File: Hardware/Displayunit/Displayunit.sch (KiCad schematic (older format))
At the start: 120 parts, among them IC1 TSC2007, IC2 MX25LM51245GXDI00, IC3 IS66WVH8M8BLL-100B1LI_0, J1 8P8C_Shielded, J2 8P8C_Shielded, J3 54104-4031, J4 Conn_ARM_JTAG_SWD_20, J5 52271-0679, J6 Conn_02x06_Odd_Even, J7 WAGO_Klemmleiste_2-pol, J8 USB_B_Micro, J9 Conn_02x05_Odd_Even, Q1 2N7002, SW1 Boot, SW2 Reset, U1 STM32L4R9ZITx, U2 USBLC6-2SC6, U3 STLD40D, U4 MAX17572, U5 MAX17572, U6 SN65HVD231, U7 AT25xxx, Y1 16 MHz, Y2 32.768

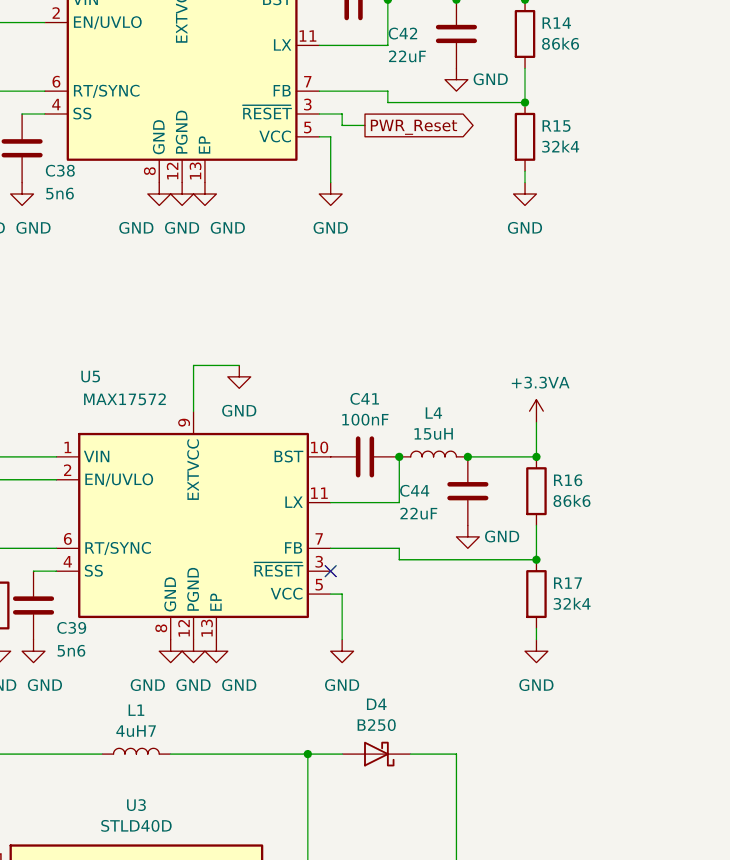
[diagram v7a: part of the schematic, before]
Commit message: Fix: behinderten Masse Bug an 3v3 Regler Mainunit und Displayboard
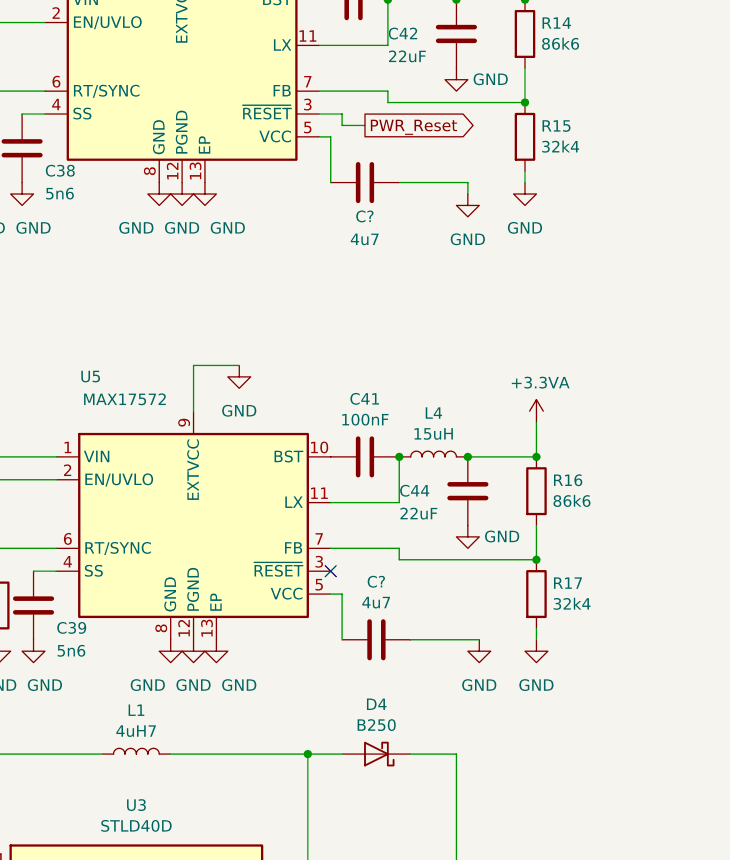
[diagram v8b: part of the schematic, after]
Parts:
- added C? (x2): 4u7, Capacitor_SMD:C_0603_1608Metric, symbol Displayunit-rescue:C-Device
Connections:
- net GND: now also C?.1, C?.1; no longer U4.5 (VCC), U5.5 (VCC)
- new net: C?.2, U4.5 (VCC)
- new net: C?.2, U5.5 (VCC)
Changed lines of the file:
@@
 EESchema Schematic File Version 4
 LIBS:Displayunit-cache
-EELAYER 29 0
+EELAYER 30 0
 EELAYER END
 $Descr A2 23386 16535
@@
 L Displayunit-rescue:GND-power #PWR?
 U 1 1 5E258B46
-P 20150 2350
+P 20750 2400
 AR Path="/5C8BBC9A/5E258B46" Ref="#PWR?"  Part="1"
 AR Path="/5E0C5EEA/5E258B46" Ref="#PWR?"  Part="1"
@@
 AR Path="/5D80E6E8/5E258B46" Ref="#PWR?"  Part="1"
 AR Path="/5E258B46" Ref="#PWR079"  Part="1"
-F 0 "#PWR079" H 20150 2100 50  0001 C CNN
-F 1 "GND" H 20150 2150 50  0000 C CNN
-F 2 "" H 20150 2350 50  0001 C CNN
-F 3 "" H 20150 2350 50  0001 C CNN
-	1    20150 2350
+F 0 "#PWR079" H 20750 2150 50  0001 C CNN
+F 1 "GND" H 20750 2200 50  0000 C CNN
+F 2 "" H 20750 2400 50  0001 C CNN
+F 3 "" H 20750 2400 50  0001 C CNN
+	1    20750 2400
 	1    0    0    -1
 $EndComp
@@
 L Displayunit-rescue:GND-power #PWR?
 U 1 1 5E258B82
-P 20200 4350
+P 20800 4350
 AR Path="/5C8BBC9A/5E258B82" Ref="#PWR?"  Part="1"
 AR Path="/5E0C5EEA/5E258B82" Ref="#PWR?"  Part="1"
@@
 AR Path="/5D80E6E8/5E258B82" Ref="#PWR?"  Part="1"
 AR Path="/5E258B82" Ref="#PWR080"  Part="1"
-F 0 "#PWR080" H 20200 4100 50  0001 C CNN
-F 1 "GND" H 20200 4150 50  0000 C CNN
-F 2 "" H 20200 4350 50  0001 C CNN
-F 3 "" H 20200 4350 50  0001 C CNN
-	1    20200 4350
+F 0 "#PWR080" H 20800 4100 50  0001 C CNN
+F 1 "GND" H 20800 4150 50  0000 C CNN
+F 2 "" H 20800 4350 50  0001 C CNN
+F 3 "" H 20800 4350 50  0001 C CNN
+	1    20800 4350
 	1    0    0    -1
 $EndComp
@@
 Wire Wire Line
 	11100 10150 11100 10250
+$Comp
+L Displayunit-rescue:C-Device C?
+U 1 1 5E2BD8A4
+P 20350 4350
+AR Path="/5C8BBC9A/5E2BD8A4" Ref="C?"  Part="1"
+AR Path="/5E0C5EEA/5E2BD8A4" Ref="C?"  Part="1"
+AR Path="/5D80EC74/5E2BD8A4" Ref="C?"  Part="1"
+AR Path="/5D80E6E8/5E2BD8A4" Ref="C?"  Part="1"
+AR Path="/5E2BD8A4" Ref="C?"  Part="1"
+F 0 "C?" V 20098 4350 50  0000 C CNN
+F 1 "4u7" V 20189 4350 50  0000 C CNN
+F 2 "Capacitor_SMD:C_0603_1608Metric" H 20388 4200 50  0001 C CNN
+F 3 "~" H 20350 4350 50  0001 C CNN
+	1    20350 4350
+	0    1    1    0
+$EndComp
+$Comp
+L Displayunit-rescue:C-Device C?
+U 1 1 5E337A65
+P 20300 2350
+AR Path="/5C8BBC9A/5E337A65" Ref="C?"  Part="1"
+AR Path="/5E0C5EEA/5E337A65" Ref="C?"  Part="1"
+AR Path="/5D80EC74/5E337A65" Ref="C?"  Part="1"
+AR Path="/5D80E6E8/5E337A65" Ref="C?"  Part="1"
+AR Path="/5E337A65" Ref="C?"  Part="1"
+F 0 "C?" V 20450 2350 50  0000 C CNN
+F 1 "4u7" V 20550 2350 50  0000 C CNN
+F 2 "Capacitor_SMD:C_0603_1608Metric" H 20338 2200 50  0001 C CNN
+F 3 "~" H 20300 2350 50  0001 C CNN
+	1    20300 2350
+	0    1    1    0
+$EndComp
+Wire Wire Line
+	20450 2350 20750 2350
+Wire Wire Line
+	20750 2350 20750 2400
+Wire Wire Line
+	20500 4350 20800 4350
 $EndSCHEMATC
